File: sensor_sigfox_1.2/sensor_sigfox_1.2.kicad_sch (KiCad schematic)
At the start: 16 parts, among them IC1 WSSFM11R2DAT, J1 Battery, J2 Conn_01x07_Socket, J3 Conn_01x01_Female, U1 ATtiny826-X, U2 MLX90393, Y1 32.768 kHz

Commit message: gerber y conexiones int/trig
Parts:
- removed J3: Conn_01x01_Female, Connector_Pin:Pin_D0.9mm_L10.0mm_W2.4mm_FlatFork, symbol Connector:Conn_01x01_Female
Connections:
- net at U1.2 (PA3): now also U2.1 (INT)
- net at U1.5 (PA4): now also U2.7 (INT/TRIG)
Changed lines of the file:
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@@
-	)
-	(junction
-		(at 224.79 86.36)
-		(diameter 0)
-		(color 0 0 0 0)
 	)
 	(junction
@@
 	(wire
 		(pts
+			(xy 138.43 88.9) (xy 138.43 101.6)
+		)
+		(stroke
+			(width 0)
+			(type default)
+		)
+	)
+	(wire
+		(pts
 			(xy 109.22 35.56) (xy 109.22 81.28)
 		)
@@
 	(wire
 		(pts
-			(xy 218.44 86.36) (xy 224.79 86.36)
+			(xy 167.64 111.76) (xy 162.56 111.76)
 		)
 		(stroke
@@
 	(wire
 		(pts
+			(xy 135.89 91.44) (xy 135.89 104.14)
+		)
+		(stroke
+			(width 0)
+			(type default)
+		)
+	)
+	(wire
+		(pts
 			(xy 156.21 143.51) (xy 156.21 133.35)
 		)
@@
 	(wire
 		(pts
+			(xy 95.25 88.9) (xy 107.95 88.9)
+		)
+		(stroke
+			(width 0)
+			(type default)
+		)
+	)
+	(wire
+		(pts
 			(xy 64.77 57.15) (xy 60.96 57.15)
 		)
@@
 	(wire
 		(pts
+			(xy 167.64 101.6) (xy 167.64 111.76)
+		)
+		(stroke
+			(width 0)
+			(type default)
+		)
+	)
+	(wire
+		(pts
 			(xy 142.24 78.74) (xy 142.24 45.72)
 		)
@@
 	(wire
 		(pts
-			(xy 224.79 86.36) (xy 224.79 85.09)
-		)
-		(stroke
-			(width 0)
-			(type default)
-		)
-	)
-	(wire
-		(pts
 			(xy 110.49 27.94) (xy 110.49 78.74)
 		)
@@
 	(wire
 		(pts
+			(xy 109.22 86.36) (xy 109.22 88.9)
+		)
+		(stroke
+			(width 0)
+			(type default)
+		)
+	)
+	(wire
+		(pts
 			(xy 218.44 78.74) (xy 220.98 78.74)
 		)
@@
 	(wire
 		(pts
+			(xy 107.95 91.44) (xy 135.89 91.44)
+		)
+		(stroke
+			(width 0)
+			(type default)
+		)
+	)
+	(wire
+		(pts
 			(xy 231.14 88.9) (xy 231.14 92.71)
 		)
@@
 	(wire
 		(pts
+			(xy 171.45 104.14) (xy 171.45 114.3)
+		)
+		(stroke
+			(width 0)
+			(type default)
+		)
+	)
+	(wire
+		(pts
 			(xy 110.49 27.94) (xy 116.84 27.94)
 		)
@@
 	(wire
 		(pts
+			(xy 171.45 114.3) (xy 162.56 114.3)
+		)
+		(stroke
+			(width 0)
+			(type default)
+		)
+	)
+	(wire
+		(pts
 			(xy 149.86 105.41) (xy 149.86 106.68)
 		)
@@
 	(wire
 		(pts
+			(xy 107.95 88.9) (xy 107.95 91.44)
+		)
+		(stroke
+			(width 0)
+			(type default)
+		)
+	)
+	(wire
+		(pts
+			(xy 135.89 104.14) (xy 171.45 104.14)
+		)
+		(stroke
+			(width 0)
+			(type default)
+		)
+	)
+	(wire
+		(pts
 			(xy 102.87 123.19) (xy 102.87 129.54)
 		)
@@
 	(wire
 		(pts
+			(xy 109.22 88.9) (xy 138.43 88.9)
+		)
+		(stroke
+			(width 0)
+			(type default)
+		)
+	)
+	(wire
+		(pts
 			(xy 102.87 17.78) (xy 102.87 21.59)
 		)
@@
 	(wire
 		(pts
-			(xy 224.79 86.36) (xy 231.14 86.36)
+			(xy 218.44 86.36) (xy 231.14 86.36)
 		)
 		(stroke
@@
 	(wire
 		(pts
+			(xy 95.25 86.36) (xy 109.22 86.36)
+		)
+		(stroke
+			(width 0)
+			(type default)
+		)
+	)
+	(wire
+		(pts
 			(xy 232.41 58.42) (xy 232.41 63.5)
 		)
@@
 		(pts
 			(xy 110.49 83.82) (xy 110.49 86.36)
+		)
+		(stroke
+			(width 0)
+			(type default)
+		)
+	)
+	(wire
+		(pts
+			(xy 138.43 101.6) (xy 167.64 101.6)
 		)
 		(stroke
@@
 					(unit 1)
 				)
-			)
-		)
-	)
-	(symbol
-		(lib_id "Connector:Conn_01x01_Female")
-		(at 224.79 80.01 90)
-		(unit 1)
-		(exclude_from_sim no)
-		(in_bom yes)
-		(on_board yes)
-		(dnp no)
-		(property "Reference" "J3"
-			(at 224.79 81.28 90)
-			(effects
-				(font
-					(size 1.27 1.27)
-				)
-				(justify right)
-			)
-		)
-		(property "Value" "Conn_01x01_Female"
-			(at 224.79 83.82 90)
-			(effects
-				(font
-					(size 1.27 1.27)
-				)
-				(justify right)
-				(hide yes)
-			)
-		)
-		(property "Footprint" "Connector_Pin:Pin_D0.9mm_L10.0mm_W2.4mm_FlatFork"
-			(at 224.79 80.01 0)
-			(effects
-				(font
-					(size 1.27 1.27)
-				)
-				(hide yes)
-			)
-		)
-		(property "Datasheet" "~"
-			(at 224.79 80.01 0)
-			(effects
-				(font
-					(size 1.27 1.27)
-				)
-				(hide yes)
-			)
-		)
-		(property "Description" ""
-			(at 224.79 80.01 0)
-			(effects
-				(font
-					(size 1.27 1.27)
-				)
-				(hide yes)
-			)
-		)
-		(pin "1"
-		)
-		(instances
-			(project "sensor_sigfox_1.2"
-				(path "/7e4087c3-8cfe-4a56-93d2-ee627c3b6019"
-					(reference "J3")
-					(unit 1)
-				)

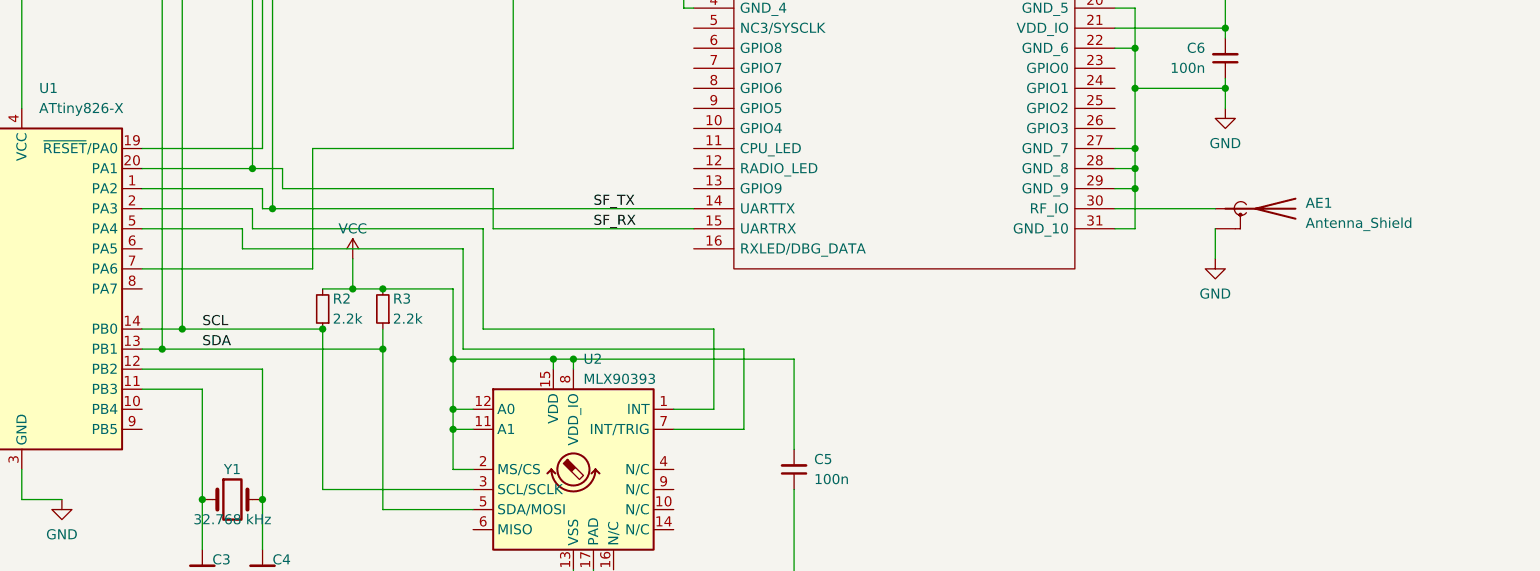
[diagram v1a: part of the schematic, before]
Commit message: 1.1 y 1.2 actualizados
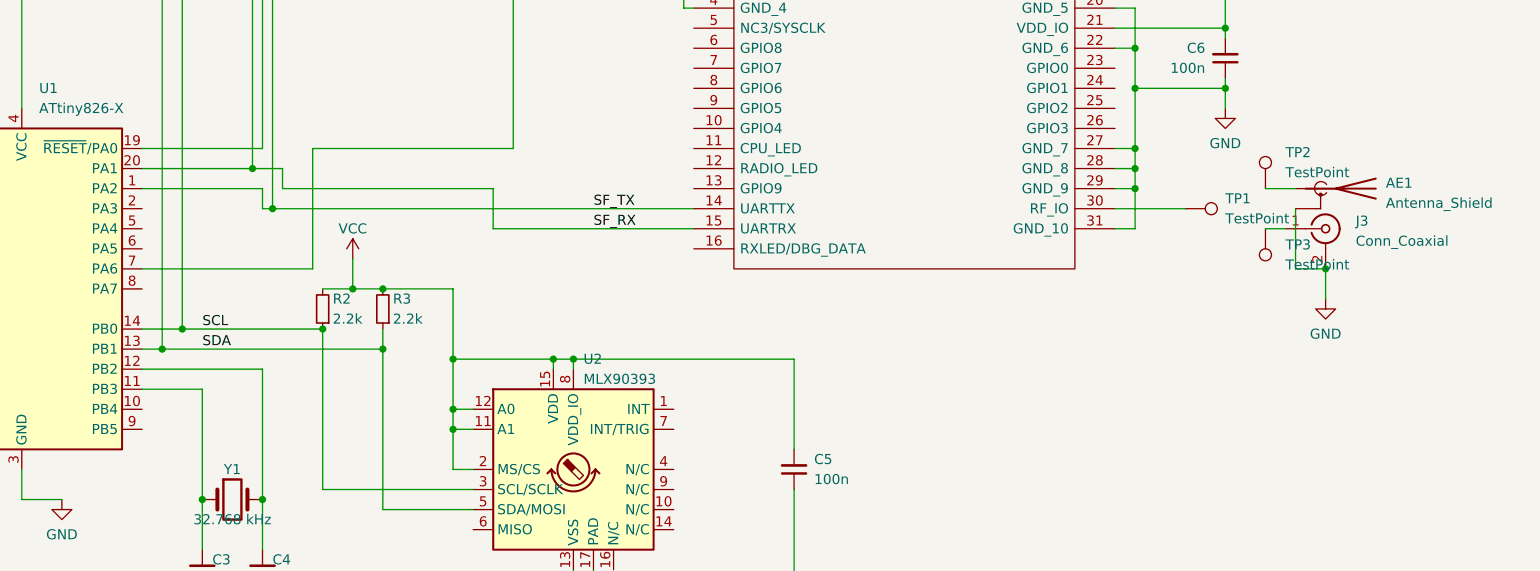
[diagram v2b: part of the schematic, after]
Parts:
- added J3: Conn_Coaxial, Connector_Coaxial:U.FL_Hirose_U.FL-R-SMT-1_Vertical, symbol Connector:Conn_Coaxial
- added TP1, TP2, TP3: TestPoint, TestPoint:TestPoint_Pad_1.0x1.0mm, symbol Connector:TestPoint
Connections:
- net GND: now also J3.2 (Ext)
- net at IC1.30 (RF_IO): now also TP1.1; no longer AE1.1 (A)
- net at U1.2 (PA3): no longer U2.1 (INT)
- net at U1.5 (PA4): no longer U2.7 (INT/TRIG)
- new net: J3.1 (In), TP3.1
- new net: AE1.1 (A), TP2.1
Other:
- moved on the sheet: AE1
